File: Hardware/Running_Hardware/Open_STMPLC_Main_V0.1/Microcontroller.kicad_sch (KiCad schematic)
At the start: 1 part, among them U2 STM32F407VGTx

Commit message: schematic updates v0.1
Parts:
- added D10, D11, D12, D13, D8, D9: LED, symbol Device:LED_Small
- added R21, R22, R23, R24, R25, R26: 470R, symbol Device:R_Small
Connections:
- net +3V3: now reaches U2.100 (VDD)
- net +3V3: now also U2.11 (VDD), U2.19 (VDD), U2.22 (VDDA), U2.28 (VDD), U2.50 (VDD), U2.75 (VDD), R21.2, R22.2, R23.2, R24.2, R25.2, R26.2
- new net: D13.2 (A), R26.1
- new net: D11.2 (A), R24.1
- new net: D8.2 (A), R21.1
- new net: D10.2 (A), R23.1
- new net: D12.2 (A), R25.1
- new net: D9.2 (A), R22.1
- new net Ethernet_Activity_LED: D12.1 (K)
- new net Ethernet_Link_LED: D11.1 (K)
- new net FAULT_LED: D10.1 (K)
- new net Internet_Status_LED: D13.1 (K)
- new net POWER_LED: D8.1 (K)
- new net RUN_LED: D9.1 (K)

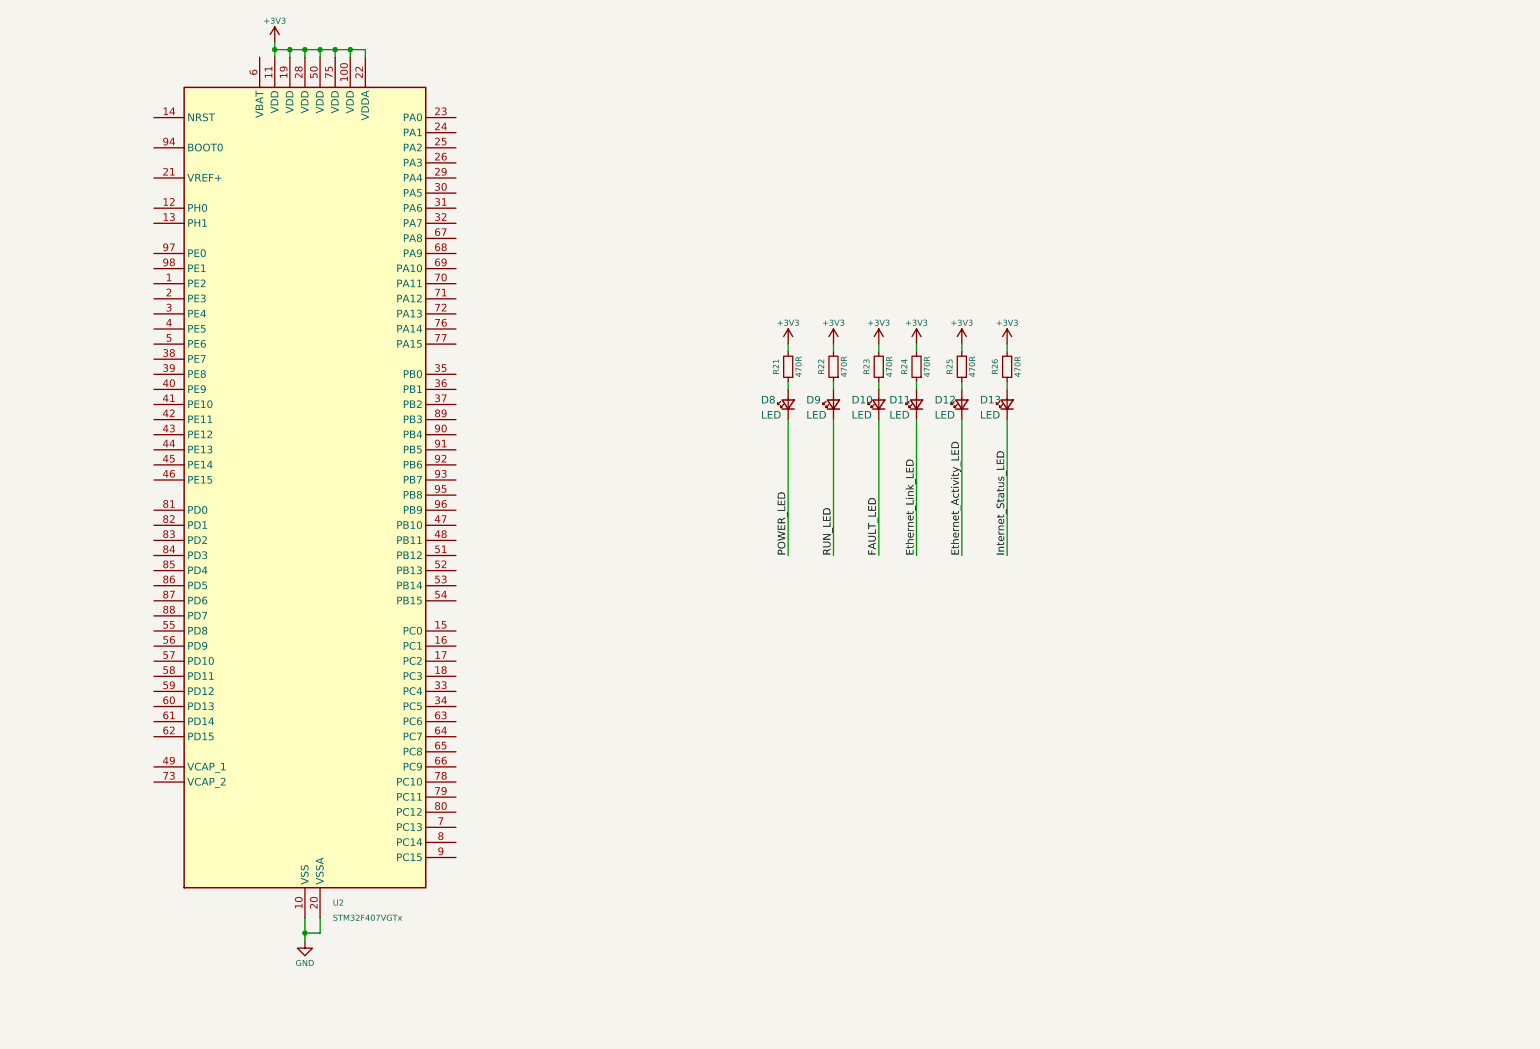
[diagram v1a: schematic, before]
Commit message: IO board schematic
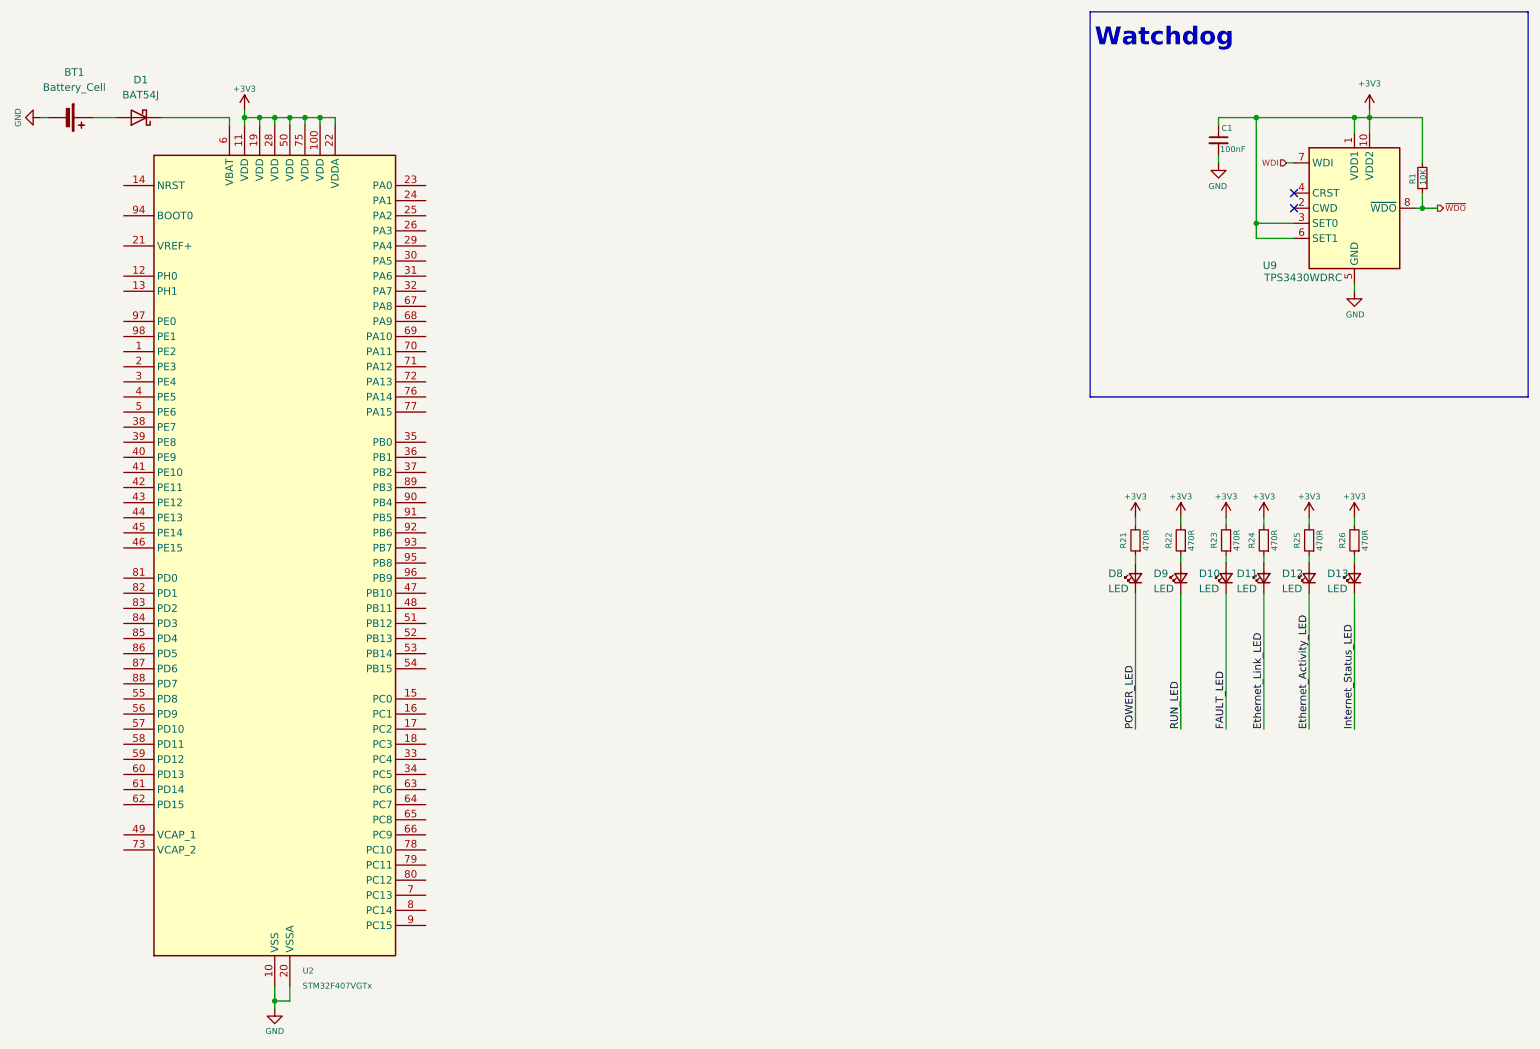
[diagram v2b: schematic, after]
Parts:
- added BT1: Battery_Cell, symbol Device:Battery_Cell
- added C1: 100nF, Capacitor_SMD:C_0603_1608Metric_Pad1.08x0.95mm_HandSolder, symbol Device:C_Small
- added D1: BAT54J, Diode_SMD:D_SOD-323F, symbol Diode:BAT54J
- added R1: 10K, Resistor_SMD:R_0603_1608Metric_Pad0.98x0.95mm_HandSolder, symbol Device:R_Small
- added U9: TPS3430WDRC, Package_SON:VSON-10-1EP_3x3mm_P0.5mm_EP1.65x2.4mm, symbol Power_Supervisor:TPS3430WDRC
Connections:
- net +3V3: now also C1.1, R1.2, U9.1 (VDD1), U9.10 (VDD2), U9.3 (SET0), U9.6 (SET1)
- net GND: now also BT1.2 (-), C1.2, U9.11 (GND), U9.5 (GND)
- net at U2.6 (VBAT): now also D1.1 (K)
- new net: BT1.1 (+), D1.2 (A)
- new net WDI: U9.7 (WDI)
- new net ~{WDO}: R1.1, U9.8 (~{WDO})
- no-connect marks 0 -> 2
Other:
- note added: "Watchdog"
- moved on the sheet: D10, D11, D12, D13, D8, D9, R21, R22, R23, R24, R25, R26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

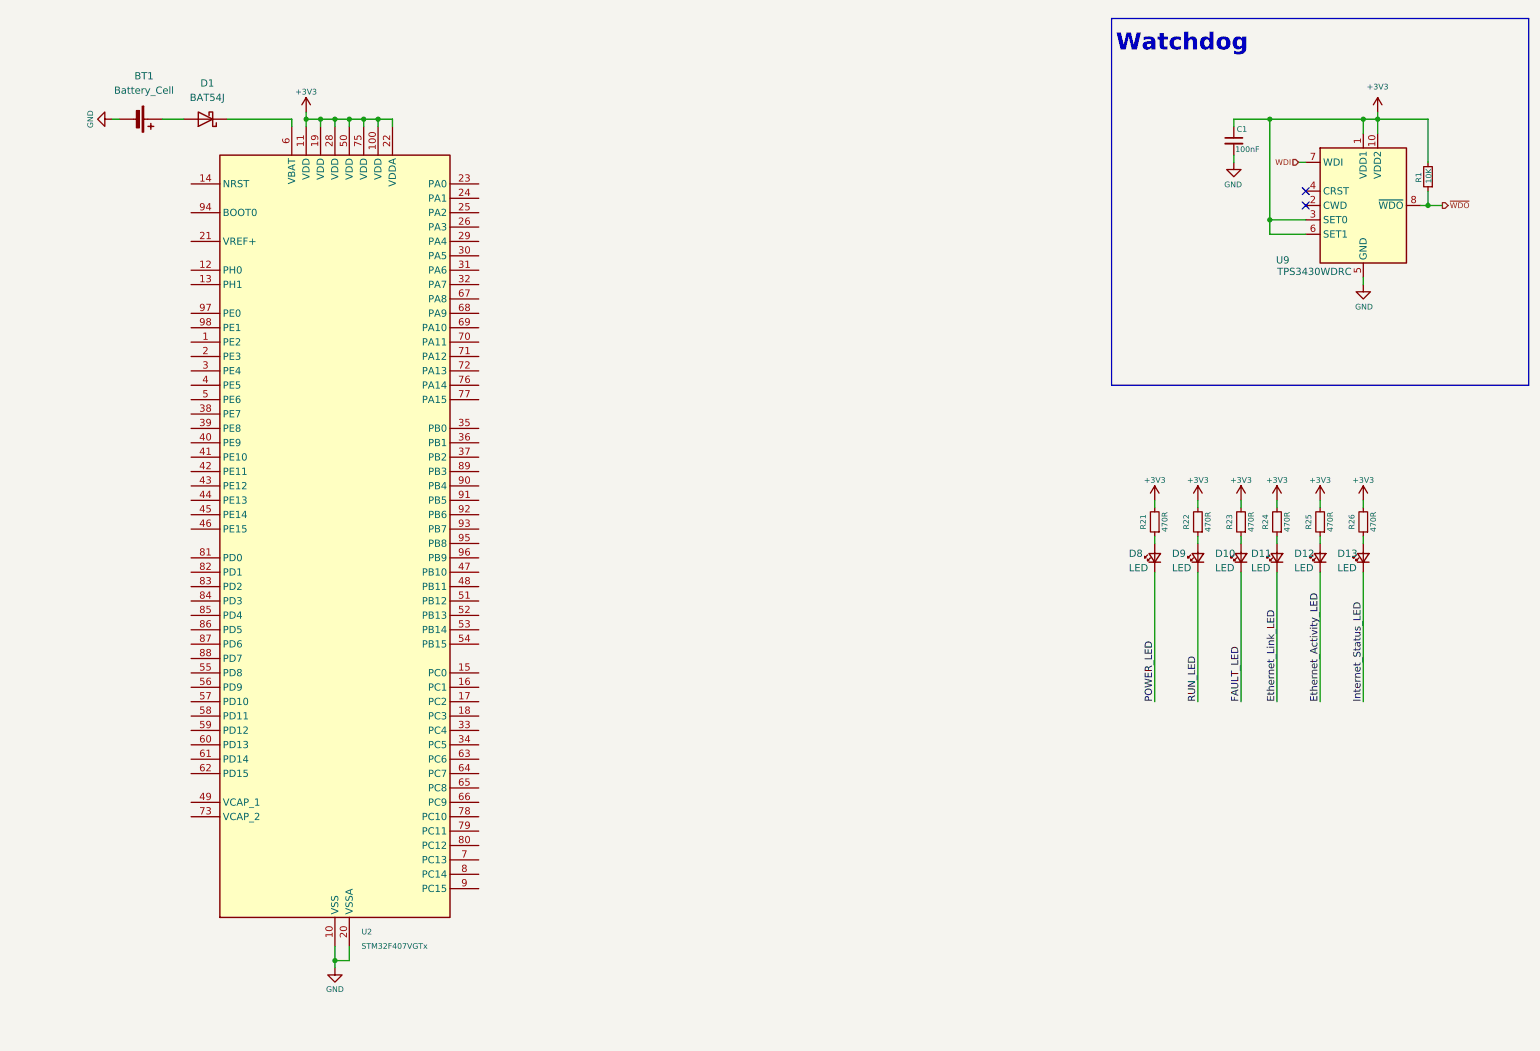
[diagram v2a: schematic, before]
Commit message: IO board schematic changes
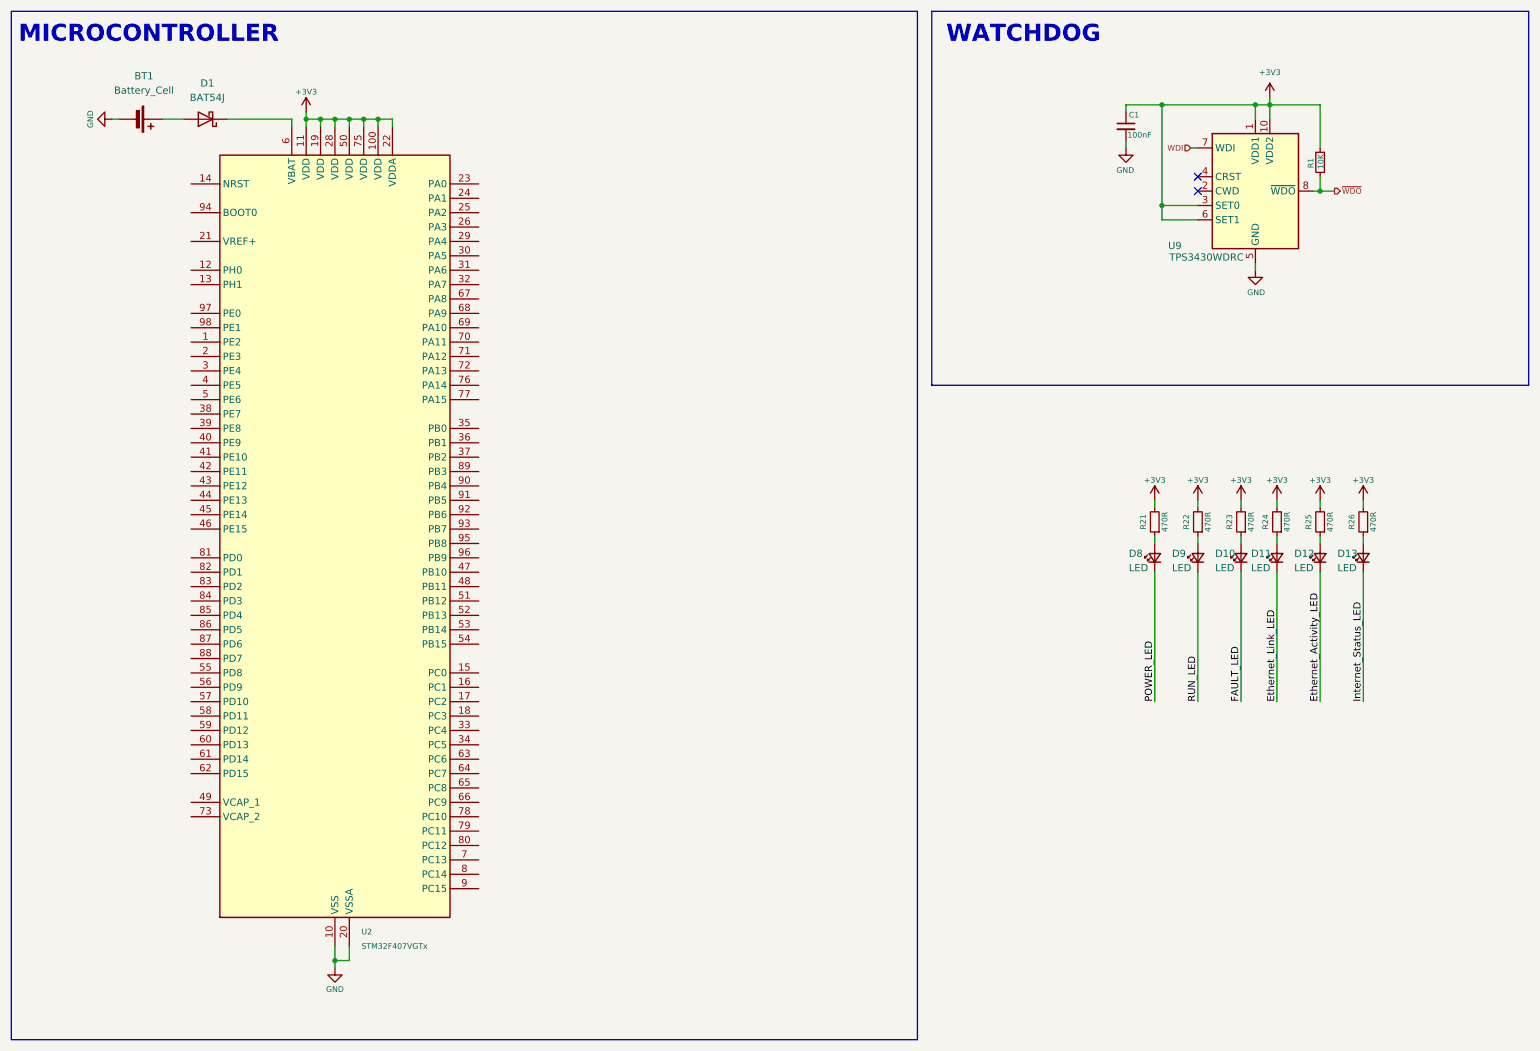
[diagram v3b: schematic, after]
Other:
- note added: "MICROCONTROLLER"
- note added: "WATCHDOG"
- note removed: "Watchdog"
- moved on the sheet: C1, R1, U9

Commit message: Main PCB schematic changes V0.1
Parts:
- removed U2: STM32F407VGTx, Package_QFP:LQFP-100_14x14mm_P0.5mm, symbol MCU_ST_STM32F4:STM32F407VGTx
- added C22: 10uF, Capacitor_SMD:C_0805_2012Metric_Pad1.18x1.45mm_HandSolder, symbol Device:C_Small
- added C27, C28, C29, C30, C31, C34, C35, C40, C41, C42, C43, C44, C45, C46: 100nF, Capacitor_SMD:C_0603_1608Metric_Pad1.08x0.95mm_HandSolder, symbol Device:C_Small
- added C47, C48, C49, C50: 10pF, Capacitor_SMD:C_0603_1608Metric_Pad1.08x0.95mm_HandSolder, symbol Device:C_Small
- added R15, R16: 10K, Resistor_SMD:R_0603_1608Metric_Pad0.98x0.95mm_HandSolder, symbol Device:R_Small
- added R3: 0R, Resistor_SMD:R_0603_1608Metric_Pad0.98x0.95mm_HandSolder, symbol Device:R_Small
- added SW3: Switch, Button_Switch_SMD:SW_SPST_PTS810, symbol Switch:SW_Push
- added U2: STM32F407ZGTx, Package_QFP:LQFP-144_20x20mm_P0.5mm, symbol MCU_ST_STM32F4:STM32F407ZGTx
- added Y1: 32.768kHz, Crystal:Crystal_SMD_3215-2Pin_3.2x1.5mm, symbol Device:Crystal
- added Y2: 48MHz, Crystal:Crystal_SMD_5032-4Pin_5.0x3.2mm, symbol Device:Crystal_GND24
- D10, D11, D12, D13, D8, D9: footprint (none) -> LED_SMD:LED_0603_1608Metric_Pad1.05x0.95mm_HandSolder
- R21, R22, R23, R24, R25, R26: footprint (none) -> Resistor_SMD:R_0603_1608Metric_Pad0.98x0.95mm_HandSolder
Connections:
- net +3V3: now also R3.1
- net GND: now also C22.2, C27.2, C28.2, C29.2, C30.2, C31.2, C34.2, C35.2, C40.2, C41.2, C42.2, C43.2, C44.2, C45.2, C46.2, C47.2, C48.2, C49.2, C50.2, R16.1, SW3.1, U2.107 (VSS), U2.120 (VSS), U2.130 (VSS), U2.16 (VSS), U2.31 (VSSA), U2.38 (VSS), U2.51 (VSS), U2.61 (VSS), U2.83 (VSS), U2.94 (VSS), Y2.2, Y2.4
- net at D1.1 (K): now also U2.6 (VBAT)
- new net: C48.1, U2.24 (PH1), Y2.1
- new net: C22.1, C27.1, C28.1, C29.1, C30.1, C31.1, C34.1, C35.1, C40.1, C41.1, C42.1, C43.1, C44.1, C45.1, R15.1, R3.2, U2.108 (VDD), U2.121 (VDD), U2.131 (VDD), U2.144 (VDD), U2.17 (VDD), U2.30 (VDD), U2.33 (VDDA), U2.39 (VDD), U2.52 (VDD), U2.62 (VDD), U2.72 (VDD), U2.84 (VDD), U2.95 (VDD)
- new net: R16.2, U2.138 (BOOT0)
- new net: C47.1, U2.23 (PH0), Y2.3
- new net: C46.1, R15.2, SW3.2, U2.25 (NRST)
- new net: C49.1, U2.8 (PC14), Y1.2
- new net: C50.1, U2.9 (PC15), Y1.1
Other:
- title: (none) -> Open_STMPLC_Main
- moved on the sheet: BT1, C1, D1, D10, D11, D12, D13, D8, D9, R1, R21, R22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
